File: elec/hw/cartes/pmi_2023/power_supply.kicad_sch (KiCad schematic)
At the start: 46 parts, among them J5 254, J8 254, Q3 DMP2008UFG-7, SW8 MSS12C02LS-BB2.0, U28 TLV61070A, U29 TLV61070A, U33 TLV61070A, U34 TLV61070A, U35 LDL1117S33R

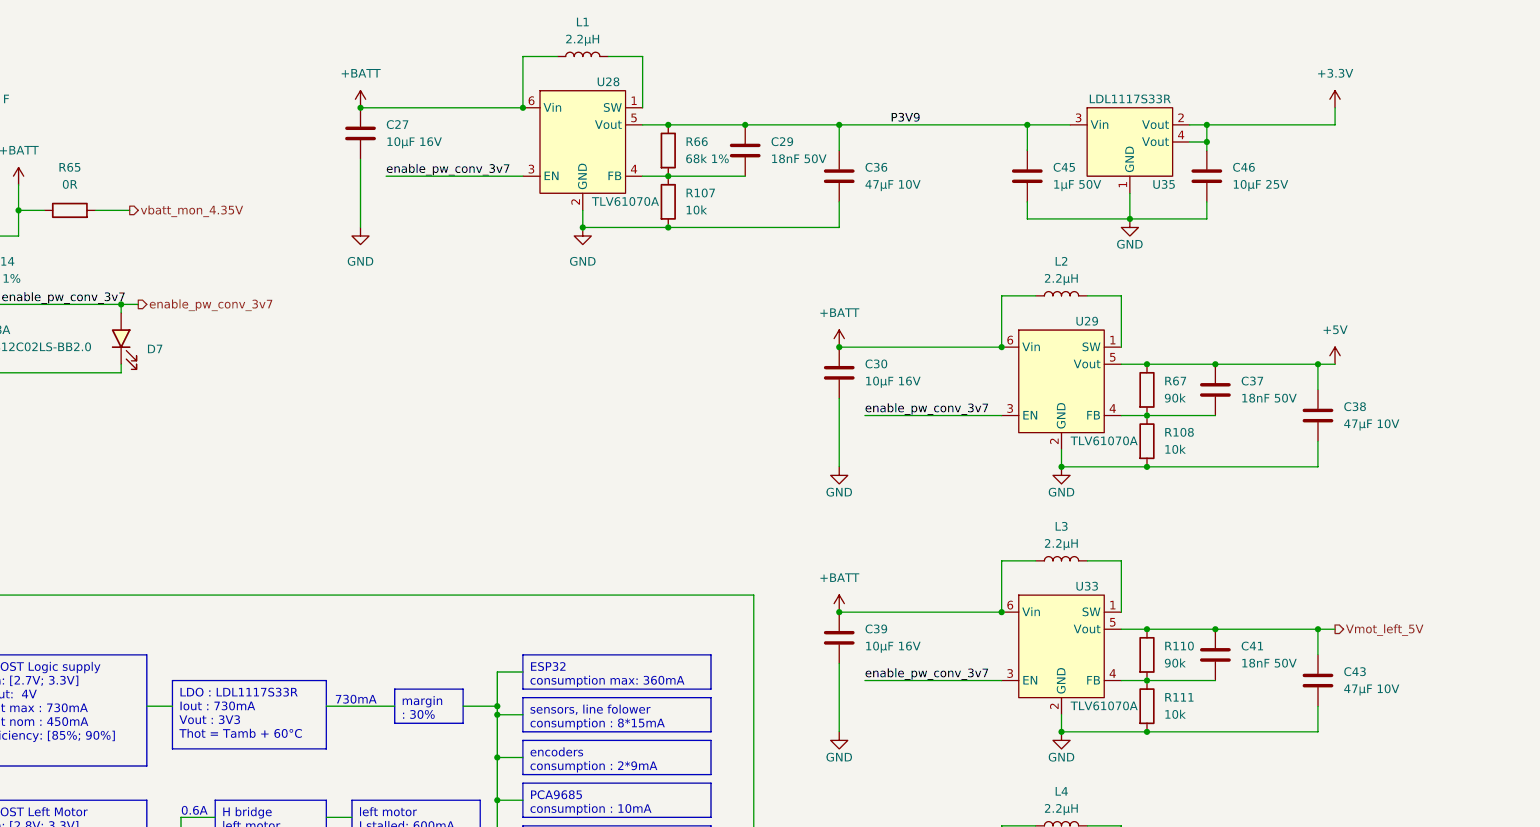
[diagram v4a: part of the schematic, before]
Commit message: pmi layout (WIP)
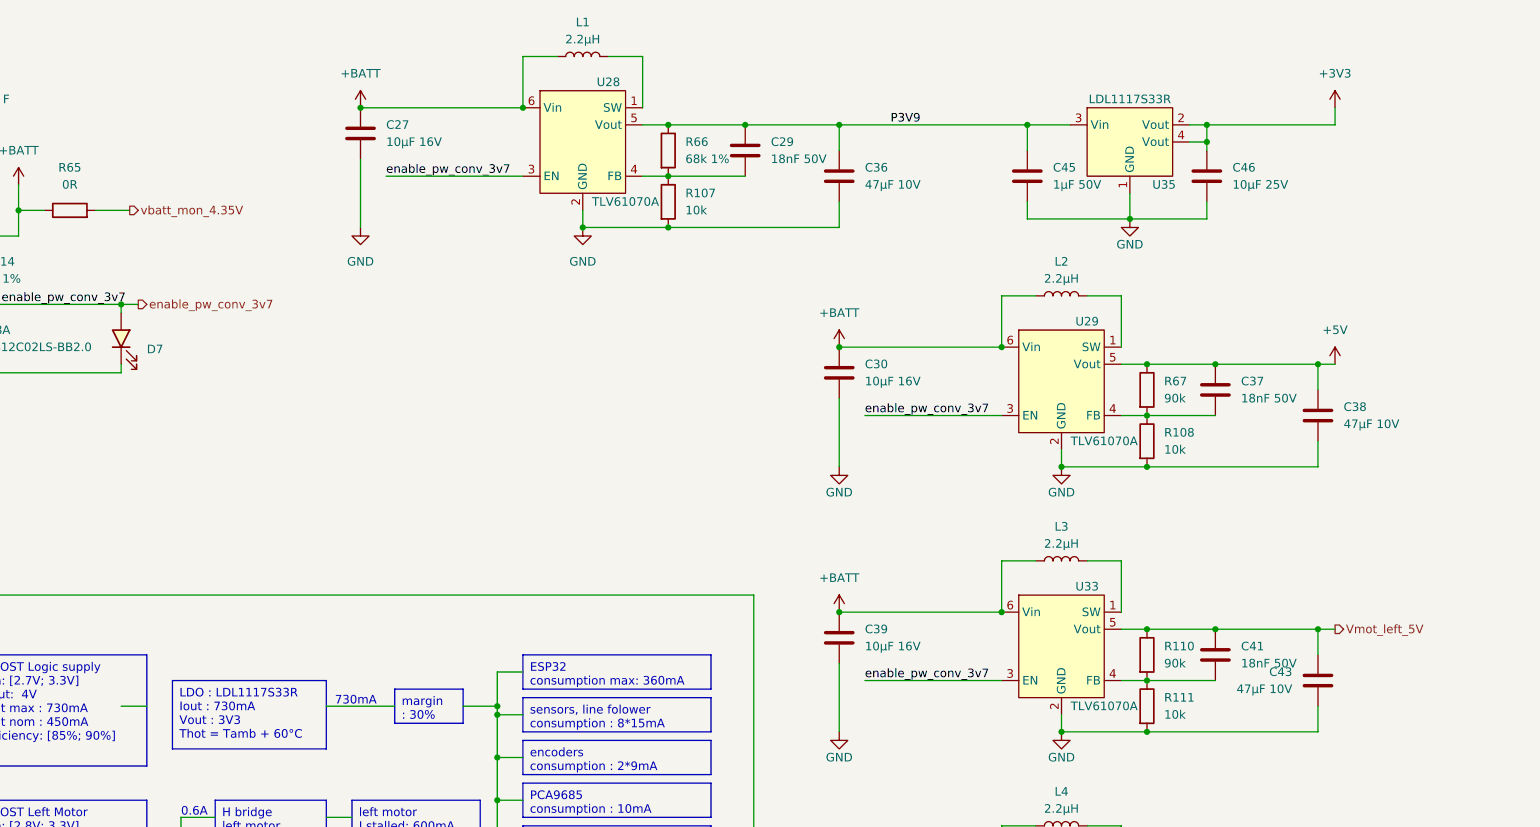
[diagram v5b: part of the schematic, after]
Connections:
- net +3.3V renamed +3V3
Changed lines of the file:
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@@
     (stroke (width 0) (type default))
   )
-  (wire (pts (xy 86.36 116.84) (xy 90.17 116.84))
+  (wire (pts (xy 86.36 116.84) (xy 82.55 116.84))
     (stroke (width 0) (type default))
   )
@@
     (effects (font (size 1.27 1.27)) (justify left))
   )
-  (symbol (lib_id "power:+3.3V") (at 262.89 27.94 0) (unit 1)
-    (in_bom yes) (on_board yes) (dnp no) (fields_autoplaced)
-    (property "Reference" "#PWR017" (at 262.89 31.75 0)
-      (effects (font (size 1.27 1.27)) hide)
-    )
-    (property "Value" "+3.3V" (at 262.89 22.86 0)
-      (effects (font (size 1.27 1.27)))
-    )
-    (property "Footprint" "" (at 262.89 27.94 0)
-      (effects (font (size 1.27 1.27)) hide)
-    )
-    (property "Datasheet" "" (at 262.89 27.94 0)
-      (effects (font (size 1.27 1.27)) hide)
-    )
-    (pin "1")
-    (instances
-      (project "pmi_2023"
-        (path "/334a657f-c66c-4260-9567-14f1c99913d7/5ea42701-5087-46e6-be28-1d7732af67f5"
-          (reference "#PWR017") (unit 1)
-        )
-      )
-    )
-  )
   (symbol (lib_id "cocotter_others:JFC2410-2100FS") (at 55.88 26.67 0) (unit 1)
     (in_bom yes) (on_board yes) (dnp no)
@@
     )
   )
+  (symbol (lib_id "power:+3V3") (at 262.89 27.94 0) (unit 1)
+    (in_bom yes) (on_board yes) (dnp no) (fields_autoplaced)
+    (property "Reference" "#PWR031" (at 262.89 31.75 0)
+      (effects (font (size 1.27 1.27)) hide)
+    )
+    (property "Value" "+3V3" (at 262.89 22.86 0)
+      (effects (font (size 1.27 1.27)))
+    )
+    (property "Footprint" "" (at 262.89 27.94 0)
+      (effects (font (size 1.27 1.27)) hide)
+    )
+    (property "Datasheet" "" (at 262.89 27.94 0)
+      (effects (font (size 1.27 1.27)) hide)
+    )
+    (pin "1")
+    (instances
+      (project "pmi_2023"
+        (path "/334a657f-c66c-4260-9567-14f1c99913d7/5ea42701-5087-46e6-be28-1d7732af67f5"
+          (reference "#PWR031") (unit 1)
+        )
+      )
+    )
+  )
   (symbol (lib_id "cocotter_connectors:254") (at 29.21 67.31 0) (unit 1)
     (in_bom yes) (on_board yes) (dnp no)
@@
     )
   )
-  (symbol (lib_id "cocotter_capacitors:C_47µF_10V_1206_X5R") (at 260.35 113.03 0) (unit 1)
-    (in_bom yes) (on_board yes) (dnp no) (fields_autoplaced)
-    (property "Reference" "C43" (at 264.16 111.76 0)
+  (symbol (lib_id "cocotter_capacitors:C_47µF_10V_1206_X5R") (at 260.35 113.03 0) (mirror y) (unit 1)
+    (in_bom yes) (on_board yes) (dnp no)
+    (property "Reference" "C43" (at 256.54 111.76 0)
       (effects (font (size 1.27 1.27)) (justify left))
     )
-    (property "Value" "47µF 10V" (at 264.16 114.3 0)
+    (property "Value" "47µF 10V" (at 256.54 114.3 0)
       (effects (font (size 1.27 1.27)) (justify left))
     )
-    (property "Footprint" "cocotter_capacitors:C_1206_3216Metric" (at 261.3152 116.84 0)
+    (property "Footprint" "cocotter_capacitors:C_1206_3216Metric" (at 259.3848 116.84 0)
       (effects (font (size 1.27 1.27)) hide)
     )

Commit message: front and back tof added, selector changed, ready to route
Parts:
- R103, R104, R105, R106, R65: JLCPCB C21189 -> C431718

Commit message: wip
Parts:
- R114: Specification 1k 0603 1% 100mW -> 10k 0603 1% 100mW; mouser (none) -> 603-RC0603FR-10100KL
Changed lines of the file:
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@@
 			)
 		)
-		(property "Description" ""
+		(property "Description" "Power symbol creates a global label with name \"+BATT\""
 			(at 189.23 63.5 0)
 			(effects
@@
 			)
 		)
-		(property "Description" ""
+		(property "Description" "Unpolarized capacitor"
 			(at 118.11 31.75 0)
 			(effects
@@
 			)
 		)
-		(property "Description" ""
+		(property "Description" "Resistor"
 			(at 74.93 43.18 0)
 			(effects
@@
 			)
 		)
-		(property "Description" ""
+		(property "Description" "Power symbol creates a global label with name \"+5V\""
 			(at 262.89 66.04 0)
 			(effects
@@
 			)
 		)
-		(property "Description" ""
+		(property "Description" "Power symbol creates a global label with name \"GND\" , ground"
 			(at 118.11 45.72 0)
 			(effects
@@
 			)
 		)
-		(property "Description" ""
+		(property "Description" "Power symbol creates a global label with name \"+3V3\""
 			(at 262.89 27.94 0)
 			(effects
@@
 			)
 		)
-		(property "Description" ""
+		(property "Description" "Power symbol creates a global label with name \"+BATT\""
 			(at 189.23 102.87 0)
 			(effects
@@
 			)
 		)
-		(property "Description" ""
+		(property "Description" "Resistor"
 			(at 55.88 31.75 0)
 			(effects
@@
 			)
 		)
-		(property "Description" ""
+		(property "Description" "Resistor"
 			(at 163.83 41.91 0)
 			(effects
@@
 			)
 		)
-		(property "Description" ""
+		(property "Description" "Resistor"
 			(at 234.95 156.21 0)
 			(effects
@@
 			)
 		)
-		(property "Description" ""
+		(property "Description" "Power symbol creates a global label with name \"+BATT\""
 			(at 118.11 27.94 0)
 			(effects
@@
 			)
 		)
-		(property "Description" ""
+		(property "Description" "Unpolarized capacitor"
 			(at 189.23 106.68 0)
 			(effects
@@
 			)
 		)
-		(property "Description" ""
+		(property "Description" "Power symbol creates a global label with name \"+BATT\""
 			(at 67.31 39.37 0)
 			(effects
@@
 			)
 		)
-		(property "Description" ""
+		(property "Description" "Power symbol creates a global label with name \"+BATT\""
 			(at 189.23 142.24 0)
 			(effects
@@
 			)
 		)
-		(property "Description" ""
+		(property "Description" "Power symbol creates a global label with name \"GND\" , ground"
 			(at 232.41 44.45 0)
 			(effects
@@
 			)
 		)
-		(property "Description" ""
+		(property "Description" "Power symbol creates a global label with name \"GND\" , ground"
 			(at 222.25 160.02 0)
 			(effects
@@
 			)
 		)
-		(property "Description" ""
+		(property "Description" "Resistor"
 			(at 234.95 77.47 0)
 			(effects
@@
 			)
 		)
-		(property "Description" ""
+		(property "Description" "Power symbol creates a global label with name \"GND\" , ground"
 			(at 222.25 120.65 0)
 			(effects
@@
 			)
 		)
-		(property "Description" ""
+		(property "Description" "Unpolarized capacitor"
 			(at 189.23 67.31 0)
 			(effects
@@
 			)
 		)
-		(property "Description" ""
+		(property "Description" "Resistor"
 			(at 234.95 116.84 0)
 			(effects
@@
 			)
 		)
-		(property "Description" ""
+		(property "Description" "Power symbol creates a global label with name \"GND\" , ground"
 			(at 222.25 81.28 0)
 			(effects
@@
 			)
 		)
-		(property "Description" ""
+		(property "Description" "Power symbol creates a global label with name \"GND\" , ground"
 			(at 189.23 81.28 0)
 			(effects
@@
 			)
 		)
-		(property "Description" ""
+		(property "Description" "Power symbol creates a global label with name \"GND\" , ground"
 			(at 151.13 45.72 0)
 			(effects
@@
 			)
 		)
-		(property "Description" ""
+		(property "Description" "Unpolarized capacitor"
 			(at 189.23 146.05 0)
 			(effects
@@
 			)
 		)
-		(property "Description" ""
+		(property "Description" "Resistor"
 			(at 55.88 46.99 0)
 			(effects
@@
 			)
 		)
-		(property "Description" ""
+		(property "Description" "Power symbol creates a global label with name \"GND\" , ground"
 			(at 189.23 120.65 0)
 			(effects
@@
 			)
 		)
-		(property "Description" ""
+		(property "Description" "Power symbol creates a global label with name \"GND\" , ground"
 			(at 29.21 69.85 0)
 			(effects
@@
 			)
 		)
-		(property "Description" ""
+		(property "Description" "Resistor"
 			(at 55.88 36.83 0)
 			(effects
@@
 			)
 		)
-		(property "Description" ""
+		(property "Description" "Resistor"
 			(at 55.88 41.91 0)
 			(effects
@@
 			)
 		)
-		(property "Description" ""
+		(property "Description" "Single-cell battery"
 			(at 26.67 63.5 0)
 			(effects
@@
 			)
 		)
-		(property "Description" ""
+		(property "Description" "Resistor"
 			(at 59.69 52.07 0)
 			(effects
@@
 			)
 		)
-		(property "Specification" "1k 0603 1% 100mW"
+		(property "Specification" "10k 0603 1% 100mW"
 			(at 59.69 52.07 0)
 			(effects
@@
 			)
 		)
-		(property "mouser" ""
+		(property "mouser" "603-RC0603FR-10100KL"
 			(at 59.69 52.07 0)
 			(effects
@@
 			)
 		)
-		(property "Description" ""
+		(property "Description" "Power symbol creates a global label with name \"GND\" , ground"
 			(at 189.23 160.02 0)
 			(effects

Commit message: wip
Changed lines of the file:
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@@
 	(wire
 		(pts
-			(xy 86.36 116.84) (xy 82.55 116.84)
-		)
-		(stroke
-			(width 0)
-			(type default)
-		)
-	)
-	(wire
-		(pts
 			(xy 189.23 102.87) (xy 213.36 102.87)
 		)
@@
 	(wire
 		(pts
+			(xy 86.36 116.84) (xy 90.17 116.84)
+		)
+		(stroke
+			(width 0)
+			(type default)
+		)
+	)
+	(wire
+		(pts
 			(xy 142.24 20.32) (xy 147.32 20.32)
 		)
@@
 	(text_box "LDO : LDL1117S33R\nIout : 730mA\nVout : 3V3\nThot = Tamb + 60°C"
 		(exclude_from_sim no)
-		(at 90.17 113.03 0)
+		(at 90.17 111.76 0)
 		(size 22.86 10.16)
 		(stroke
